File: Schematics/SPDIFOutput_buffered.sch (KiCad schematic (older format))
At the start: 4 parts, among them U5 74HC04

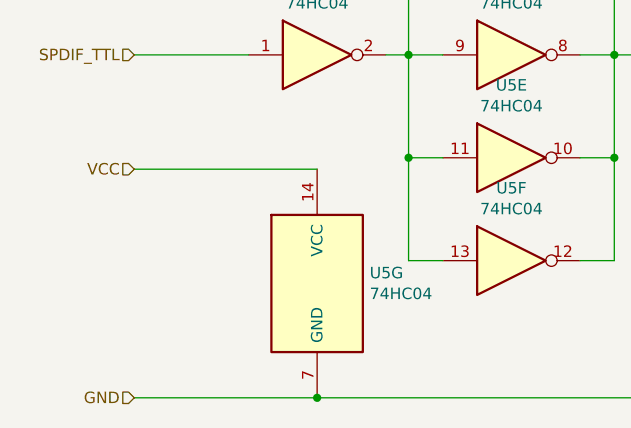
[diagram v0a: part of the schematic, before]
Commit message: Added C9 bypass capacitor; minor PCB design fixes
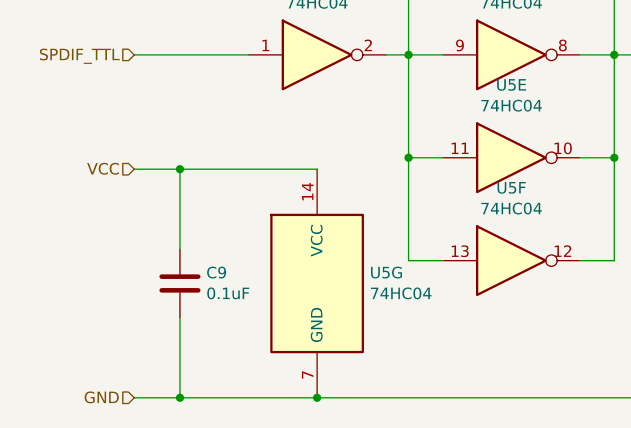
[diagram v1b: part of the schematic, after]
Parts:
- added C9: 0.1uF, Capacitor_THT:C_Disc_D5.0mm_W2.5mm_P2.50mm, symbol Device:C
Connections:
- net GND: now also C9.2
- net VCC: now also C9.1
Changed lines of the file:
@@
 Connection ~ 4950 5150
 Wire Wire Line
-	4150 5150 4950 5150
+	4150 5150 4350 5150
 Wire Wire Line
-	4150 4150 4950 4150
+	4150 4150 4350 4150
 Wire Wire Line
 	4150 3650 4650 3650
@@
 Wire Wire Line
 	7050 4200 7050 5150
+$Comp
+L Device:C C9
+U 1 1 5D4C91AD
+P 4350 4650
+F 0 "C9" H 4465 4696 50  0000 L CNN
+F 1 "0.1uF" H 4465 4605 50  0000 L CNN
+F 2 "Capacitor_THT:C_Disc_D5.0mm_W2.5mm_P2.50mm" H 4388 4500 50  0001 C CNN
+F 3 "~" H 4350 4650 50  0001 C CNN
+	1    4350 4650
+	1    0    0    -1
+$EndComp
+Wire Wire Line
+	4350 4500 4350 4150
+Connection ~ 4350 4150
+Wire Wire Line
+	4350 4150 4950 4150
+Wire Wire Line
+	4350 4800 4350 5150
+Connection ~ 4350 5150
+Wire Wire Line
+	4350 5150 4950 5150
 $EndSCHEMATC

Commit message: Minor PCB design fixes
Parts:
- R6: footprint Resistor_THT:R_Axial_DIN0207_L6.3mm_D2.5mm_P10.16mm_Horizontal -> Resistor_THT:R_Axial_DIN0309_L9.0mm_D3.2mm_P12.70mm_Horizontal
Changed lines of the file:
@@
 F 0 "R6" H 7120 4096 50  0000 L CNN
 F 1 "110" H 7120 4005 50  0000 L CNN
-F 2 "Resistor_THT:R_Axial_DIN0207_L6.3mm_D2.5mm_P10.16mm_Horizontal" V 6980 4050 50  0001 C CNN
+F 2 "Resistor_THT:R_Axial_DIN0309_L9.0mm_D3.2mm_P12.70mm_Horizontal" V 6980 4050 50  0001 C CNN
 F 3 "~" H 7050 4050 50  0001 C CNN
 	1    7050 4050

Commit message: Updated schematic and PCB design (minor modifications on layout)
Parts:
- R6: footprint Resistor_THT:R_Axial_DIN0309_L9.0mm_D3.2mm_P12.70mm_Horizontal -> Resistor_THT:R_Axial_DIN0207_L6.3mm_D2.5mm_P10.16mm_Horizontal
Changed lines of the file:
@@
 F 0 "R6" H 7120 4096 50  0000 L CNN
 F 1 "110" H 7120 4005 50  0000 L CNN
-F 2 "Resistor_THT:R_Axial_DIN0309_L9.0mm_D3.2mm_P12.70mm_Horizontal" V 6980 4050 50  0001 C CNN
+F 2 "Resistor_THT:R_Axial_DIN0207_L6.3mm_D2.5mm_P10.16mm_Horizontal" V 6980 4050 50  0001 C CNN
 F 3 "~" H 7050 4050 50  0001 C CNN
 	1    7050 4050
